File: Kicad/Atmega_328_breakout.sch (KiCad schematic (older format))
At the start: 75 parts, among them J1 Jack-DC, J10 Conn_01x06, J11 01x03, J12 01x03, J13 01x03, J14 01x03, J15 01x03, J16 01x03, J17 01x03, J18 01x03, J19 Power_connector, J2 01x03, J20 ADC_Connector, J21 PORB++_connector, J22 PORD_connector, J23 Conn_01x01, J24 Device_Connector, J25 Pin out, J26 Com_header, J27 Power terminal, J28 USB, J3 01x03, J4 01x03, J5 01x03, J6 01x03, J7 01x03, J8 01x03, J9 01x03, Q1 AO3401A, SW1 SW_Push, SW2 SW_Push, U1 NCP1117-5, U2 L7805, U3 LM358, U4 ATMEGA328P-AU, U5 MCP1700-33, U6 CH340E, Y1 Crystal_GND24

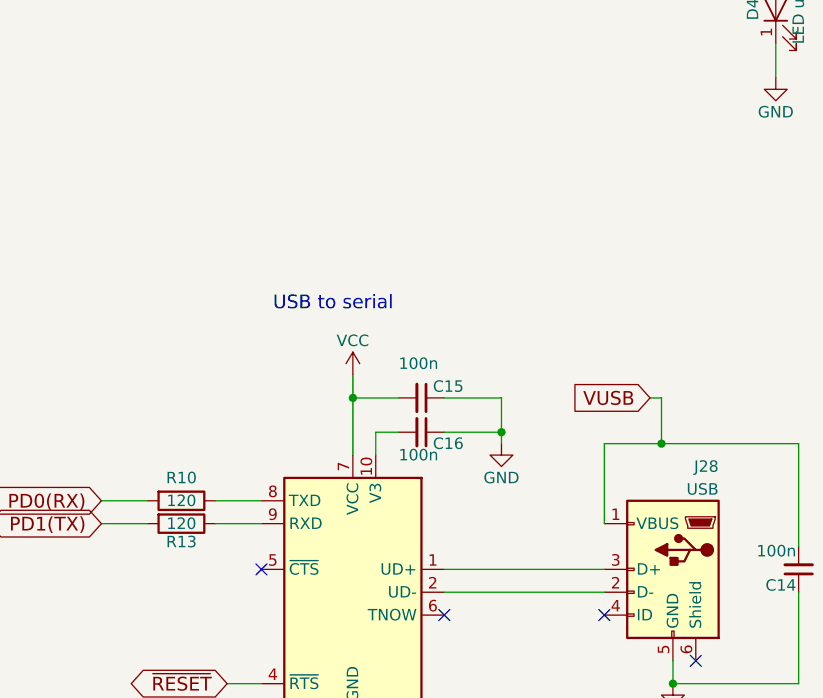
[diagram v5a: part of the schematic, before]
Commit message: replaced serial to usb chip and added safety.
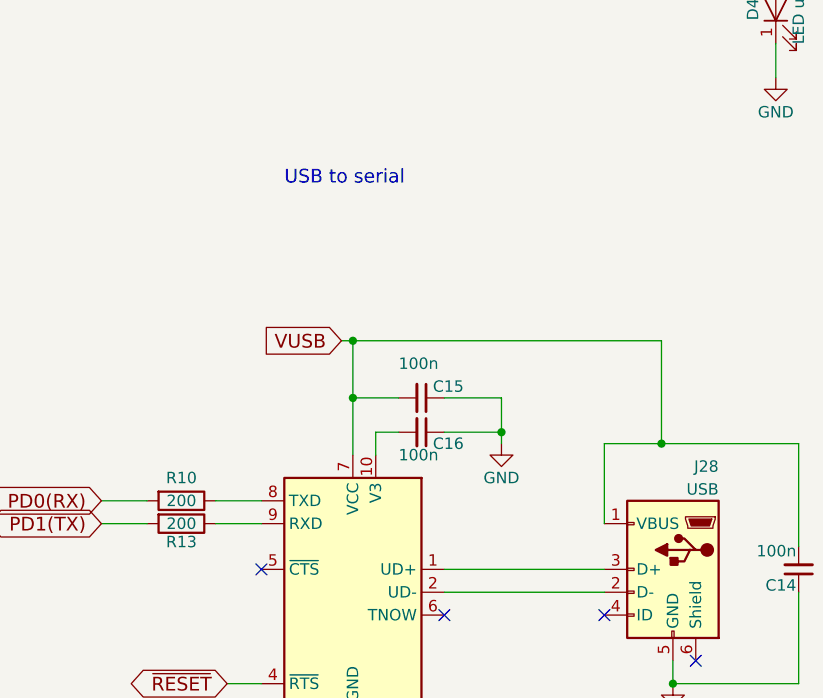
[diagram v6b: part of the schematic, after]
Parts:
- C14: footprint Capacitor_SMD:C_0603_1608Metric_Pad1.08x0.95mm_HandSolder -> Capacitor_SMD:C_0402_1005Metric; LCSC (none) -> C1525
- C15, C16: LCSC C14663 -> C1525
- D3: LCSC C2296 -> C2297
- R10, R13: value 120 -> 200; LCSC C23138 -> C25087
- U4: LCSC C132230 -> C14877
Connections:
- net VCC: no longer C15.2, U6.7 (VCC)
- net VUSB: now also C15.2, U6.7 (VCC)
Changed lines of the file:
@@
 F 2 "Package_QFP:TQFP-32_7x7mm_P0.8mm" H 3150 4350 50  0001 C CIN
 F 3 "" H 3150 4350 50  0001 C CNN
-F 4 "C132230" H 3150 4350 50  0001 C CNN "LCSC"
+F 4 "C14877" H 3150 4350 50  0001 C CNN "LCSC"
 	1    3150 4350
 	1    0    0    -1
@@
 F 0 "C14" H 14010 8870 50  0000 L CNN
 F 1 "100n" H 14010 8720 50  0000 L CNN
-F 2 "Capacitor_SMD:C_0603_1608Metric_Pad1.08x0.95mm_HandSolder" H 14000 8800 50  0001 C CNN
+F 2 "Capacitor_SMD:C_0402_1005Metric" H 14000 8800 50  0001 C CNN
 F 3 "" H 14000 8800 50  0001 C CNN
+F 4 "C1525" H 14000 8800 50  0001 C CNN "LCSC"
 	1    14000 8800
 	-1   0    0    1
@@
 Wire Wire Line
 	10750 2000 10750 2050
-Text GLabel 13350 8050 0    60   Input ~ 0
+Text GLabel 12000 7800 0    60   Input ~ 0
 VUSB
 $Comp
@@
 F 2 "LED_SMD:LED_0805_2012Metric_Pad1.15x1.40mm_HandSolder" H 5100 10200 50  0001 C CNN
 F 3 "" H 5100 10200 50  0001 C CNN
-F 4 "C2296" H 5100 10200 50  0001 C CNN "LCSC"
+F 4 "C2297" H 5100 10200 50  0001 C CNN "LCSC"
 	1    5100 10200
 	0    -1   -1   0
@@
 Wire Wire Line
 	13150 8250 13150 8600
-Wire Wire Line
-	13400 8250 13400 8050
-Wire Wire Line
-	13400 8050 13350 8050
 Connection ~ 13400 8250
 Wire Wire Line
@@
 F 2 "Capacitor_SMD:C_0402_1005Metric" H 12350 8200 50  0001 C CNN
 F 3 "" H 12350 8200 50  0001 C CNN
-F 4 "C14663" H 12350 8200 50  0001 C CNN "LCSC"
+F 4 "C1525" H 12350 8200 50  0001 C CNN "LCSC"
 	1    12350 8200
 	0    1    1    0
@@
 $EndComp
 Wire Wire Line
-	12050 7950 12050 8050
-Wire Wire Line
 	11150 8600 10950 8600
 Wire Wire Line
@@
 P 11300 8600
 F 0 "R13" V 11380 8600 50  0000 C CNN
-F 1 "120" V 11300 8600 50  0000 C CNN
+F 1 "200" V 11300 8600 50  0000 C CNN
 F 2 "Resistor_SMD:R_0402_1005Metric" V 11230 8600 50  0001 C CNN
 F 3 "" H 11300 8600 50  0001 C CNN
-F 4 "C23138" V 11300 8600 50  0001 C CNN "LCSC"
+F 4 "C25087" V 11300 8600 50  0001 C CNN "LCSC"
 	1    11300 8600
 	0    1    1    0
@@
 P 11300 8500
 F 0 "R10" V 11200 8500 50  0000 C CNN
-F 1 "120" V 11300 8500 50  0000 C CNN
+F 1 "200" V 11300 8500 50  0000 C CNN
 F 2 "Resistor_SMD:R_0402_1005Metric" V 11230 8500 50  0001 C CNN
 F 3 "" H 11300 8500 50  0001 C CNN
-F 4 "C23138" V 11300 8500 50  0001 C CNN "LCSC"
+F 4 "C25087" V 11300 8500 50  0001 C CNN "LCSC"
 	1    11300 8500
 	0    1    1    0
@@
 Text GLabel 11500 9300 0    60   BiDi ~ 0
 ~RESET
-Text Notes 11700 7675 0    60   ~ 0
+Text Notes 11750 7125 0    60   ~ 0
 USB to serial\n
 $Comp
@@
 	1    0    0    -1
 $EndComp
-$Comp
-L power:VCC #PWR033
-U 1 1 5A74603E
-P 12050 7950
-F 0 "#PWR033" H 12050 7800 50  0001 C CNN
-F 1 "VCC" H 12050 8100 50  0000 C CNN
-F 2 "" H 12050 7950 50  0001 C CNN
-F 3 "" H 12050 7950 50  0001 C CNN
-	1    12050 7950
-	1    0    0    -1
-$EndComp
 Wire Wire Line
 	12250 8200 12150 8200
@@
 F 2 "Capacitor_SMD:C_0402_1005Metric" H 12350 8050 50  0001 C CNN
 F 3 "" H 12350 8050 50  0001 C CNN
-F 4 "C14663" H 12350 8050 50  0001 C CNN "LCSC"
+F 4 "C1525" H 12350 8050 50  0001 C CNN "LCSC"
 	1    12350 8050
 	0    1    1    0
@@
 Wire Wire Line
 	12250 8050 12050 8050
-Connection ~ 12050 8050
 Wire Wire Line
 	12050 8050 12050 8300
@@
 Wire Wire Line
 	11650 8500 11450 8500
+Wire Wire Line
+	12000 7800 12050 7800
+Wire Wire Line
+	12050 7800 12050 8050
+Connection ~ 12050 8050
+Wire Wire Line
+	12050 7800 13400 7800
+Connection ~ 12050 7800
+Wire Wire Line
+	13400 7800 13400 8250
 $EndSCHEMATC
